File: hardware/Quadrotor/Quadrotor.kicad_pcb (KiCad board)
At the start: 2 copper layers, 78 x 78 mm, 118 parts, among them J1 Power, J10 MotorD, J2 EX_EXM, J3 EX_SPI, J4 USB_B_Micro, J5 MCU_JTAG, J6 NRF_JA, J7 MotorA, J8 MotorC, J9 MotorB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

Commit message: PCB布板完成
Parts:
- removed TP5: SDA, TestPoint:TestPoint_Pad_D1.0mm
- removed TP6: SCL, TestPoint:TestPoint_Pad_D1.0mm
- TP4: value BAT/2 -> BAT_ADC
- moved R20 11.3 mm to (70.9, 78.1), turned to 180 degrees
- moved C13 11.2 mm to (74.9, 73.2), turned to 180 degrees
- moved C14 10.0 mm to (74.9, 72.1), turned to 180 degrees
- moved R21 9.26 mm to (72.8, 78.1), turned to 180 degrees
- moved R13 4.13 mm to (86.8, 83.3)
- moved R2 4.02 mm to (77.7, 87.3), turned to 90 degrees
- moved D1 3.58 mm to (79.6, 85.8), turned to 90 degrees
- moved TP3 3.41 mm to (82.2, 84.1)
- moved R3 3.31 mm to (74.6, 48.5), turned to 90 degrees
- moved TP10 3.23 mm to (94.0, 81.2)
- moved C17 3.22 mm to (84.9, 76.1)
- moved C16 3.22 mm to (85.9, 76.1)
- moved R15 3.20 mm to (85.8, 83.3)
- moved R14 3.06 mm to (84.8, 83.3)
- moved R9 2.64 mm to (72.1, 68.2), turned to 0 degrees
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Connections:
- U2 pad 31: Net-(C10-Pad1) -> Net-(L2-Pad2)
- U2 pad 32: Net-(L2-Pad2) -> Net-(C10-Pad1)
- U2 pad 4: Net-(R3-Pad2) -> Net-(U2-Pad4)
- U2 pad 48: Net-(U2-Pad48) -> Net-(R3-Pad2)
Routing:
- net +3V3: track 0.00 -> 150.6 mm, vias 0 -> 8
- net +BATT: track 0.00 -> 50.6 mm, vias 0 -> 41
- net /LEDF_B4: track 0.00 -> 39.3 mm, vias 0 -> 2
- net GNDD: track 0.00 -> 38.7 mm, vias 0 -> 80
- net /LEDE_D8: track 0.00 -> 37.7 mm, vias 0 -> 2
- net /MOTORD: track 0.00 -> 36.4 mm, vias 0 -> 2
- net /MOTORB: track 0.00 -> 35.8 mm, vias 0 -> 2
- net /MOTORA: track 0.00 -> 31.3 mm, vias 0 -> 2
- net /LEDD_B2: track 0.00 -> 31.1 mm, vias 0 -> 2
- net /LEDC_C15: track 0.00 -> 24.4 mm, vias 0 -> 2
- net Net-(R15-Pad2): track 0.00 -> 24.1 mm, vias 0 -> 2
- net /MOTORC: track 0.00 -> 23.6 mm, vias 0 -> 2
- net Net-(R14-Pad2): track 0.00 -> 22.4 mm, vias 0 -> 2
- net GND: track 0.00 -> 20.8 mm, vias 0 -> 55
- net /EX_I2C_SCL(B6): track 0.00 -> 19.6 mm, vias 0 -> 1
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- added copper zone on B.Cu, net +BATT
- added copper zone on F.Cu, net +BATT
- added copper zone on B.Cu, net GND
- added copper zone on F.Cu, net GND
- added copper zone on B.Cu, net GNDD
- added copper zone on F.Cu, net GNDD
- added copper zone on F.Cu, net Net-(C30-Pad2)
- added copper zone on F.Cu, net Net-(C31-Pad2)
- added copper zone on F.Cu, net Net-(C34-Pad2)
- added copper zone on F.Cu, net Net-(C35-Pad2)
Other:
- net class Default: trace_width 0.25 -> 0.2; via_dia 0.8 -> 0.6; via_drill 0.4 -> 0.3
- net class power added: clearance 0.2, trace_width 0.2, via_dia 0.6, via_drill 0.3

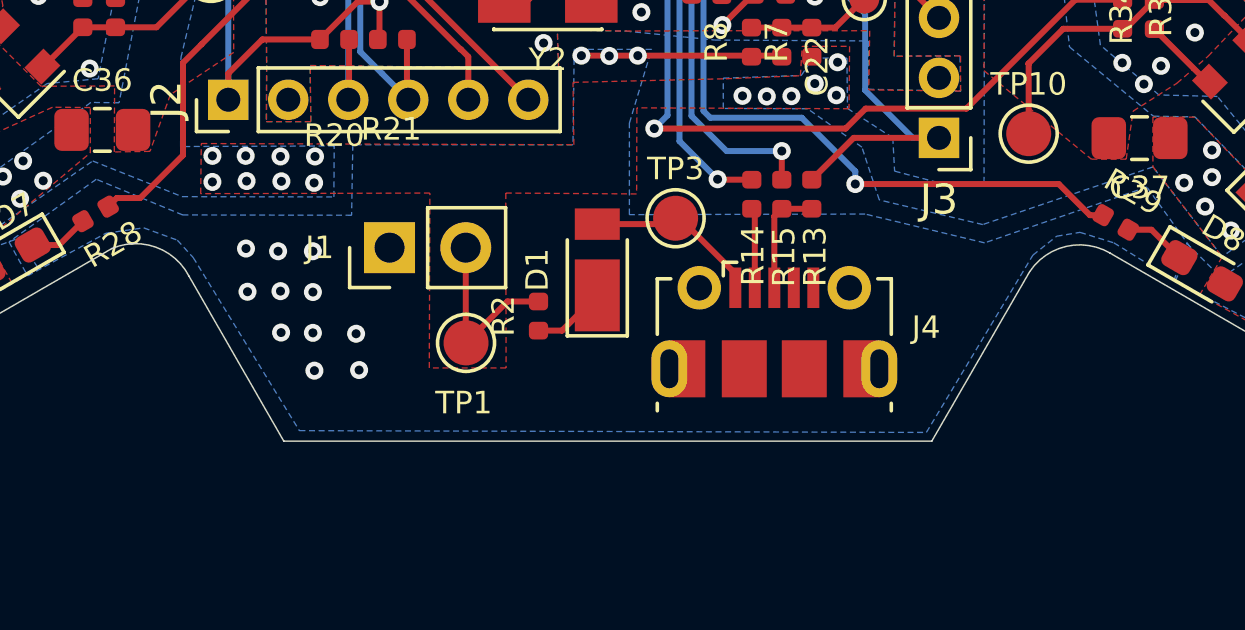
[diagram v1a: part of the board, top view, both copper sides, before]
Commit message: 添加一点覆铜地
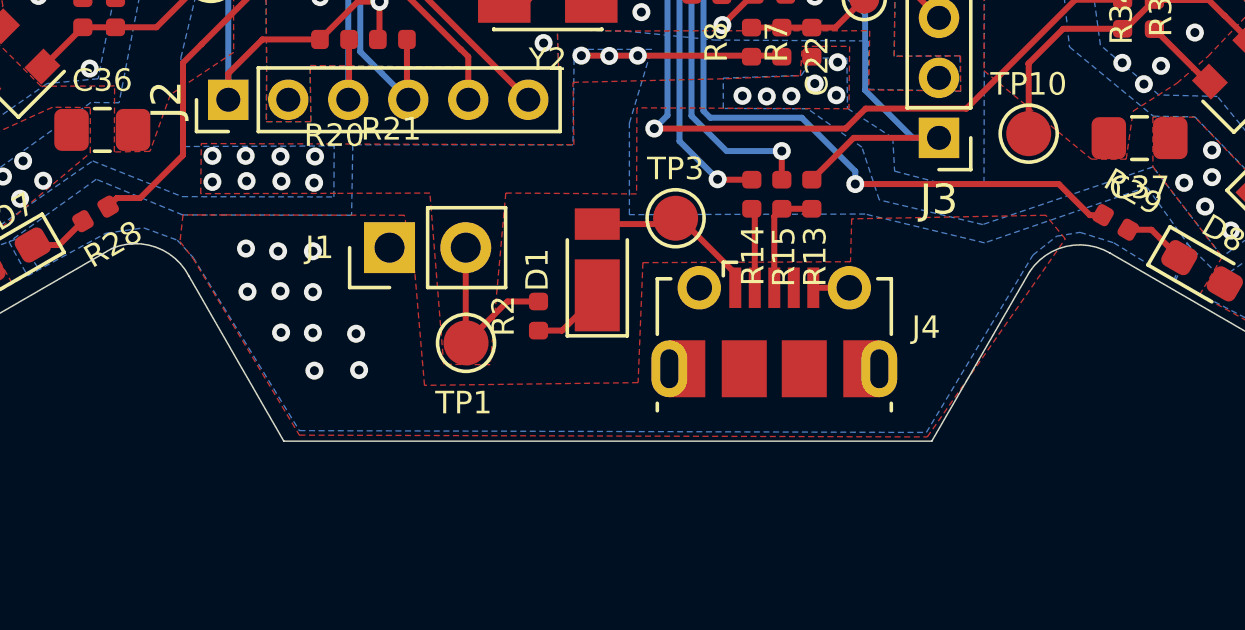
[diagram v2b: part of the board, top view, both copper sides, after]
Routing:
- net GND: track 20.8 -> 22.0 mm
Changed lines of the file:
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@@
     (thickness 1.6)
     (drawings 27)
-    (tracks 815)
+    (tracks 816)
     (zones 0)
     (modules 116)
@@
   (via (at 59.83 43.72) (size 0.6) (drill 0.3) (layers F.Cu B.Cu) (net 1))
   (via (at 60.58 44.52) (size 0.6) (drill 0.3) (layers F.Cu B.Cu) (net 1))
+  (segment (start 86.84 86.3875) (end 88.04 86.3875) (width 0.2) (layer F.Cu) (net 1))
   (segment (start 56.682947 85.007053) (end 56.682947 83.642947) (width 0.2) (layer F.Cu) (net 2))
   (segment (start 55.49 86.2) (end 56.682947 85.007053) (width 0.2) (layer F.Cu) (net 2))
@@
         (xy 70.93 83.24) (xy 66.42 83.25) (xy 66.44 81.58) (xy 78.86 81.62) (xy 78.83 79.54)
         (xy 83.93 79.42) (xy 86.41 79.32) (xy 86.47 78.34) (xy 88.05 78.34) (xy 88.03 80.42)
-        (xy 80.96 80.39) (xy 80.95 83.26) (xy 76.59 83.23) (xy 76.6 89.06) (xy 74.04 89.06)
+        (xy 80.96 80.39) (xy 80.95 83.26) (xy 76.59 83.23) (xy 76.07 88.95) (xy 74.52 88.94)
         (xy 74.06 83.23)
       )
@@
       )
     )
+  )
+  (zone (net 1) (net_name GND) (layer F.Cu) (hatch edge 0.508)
+    (connect_pads (clearance 0.508))
+    (min_thickness 0.254)
+    (fill yes (arc_segments 32) (thermal_gap 0.508) (thermal_bridge_width 0.508))
+    (polygon
+      (pts
+        (xy 65.73 84.85) (xy 66.16 85.4) (xy 69.71 91.3) (xy 90.64 91.36) (xy 95.24 84.76)
+        (xy 94.59 83.97) (xy 88.12 84.09) (xy 88.08 85.52) (xy 81.16 85.55) (xy 81 89.55)
+        (xy 73.88 89.64) (xy 73.56 85.9) (xy 73.21 83.97) (xy 67.23 83.96) (xy 66.5 83.96)
+        (xy 65.83 83.96)
+      )
+    )
